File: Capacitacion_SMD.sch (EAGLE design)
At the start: 37 parts, among them IC1 LDO3V3

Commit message: Values corrected for R7 & R8
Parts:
- R4, R5: value 22 -> 470
- R6: value 22 -> 10k
- R7, R8: value 22 -> 22k
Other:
- moved on the sheet: C1, C2, C3, C4, C5, C6, C7, IC1, ISP1, JP1, JP2, LED1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

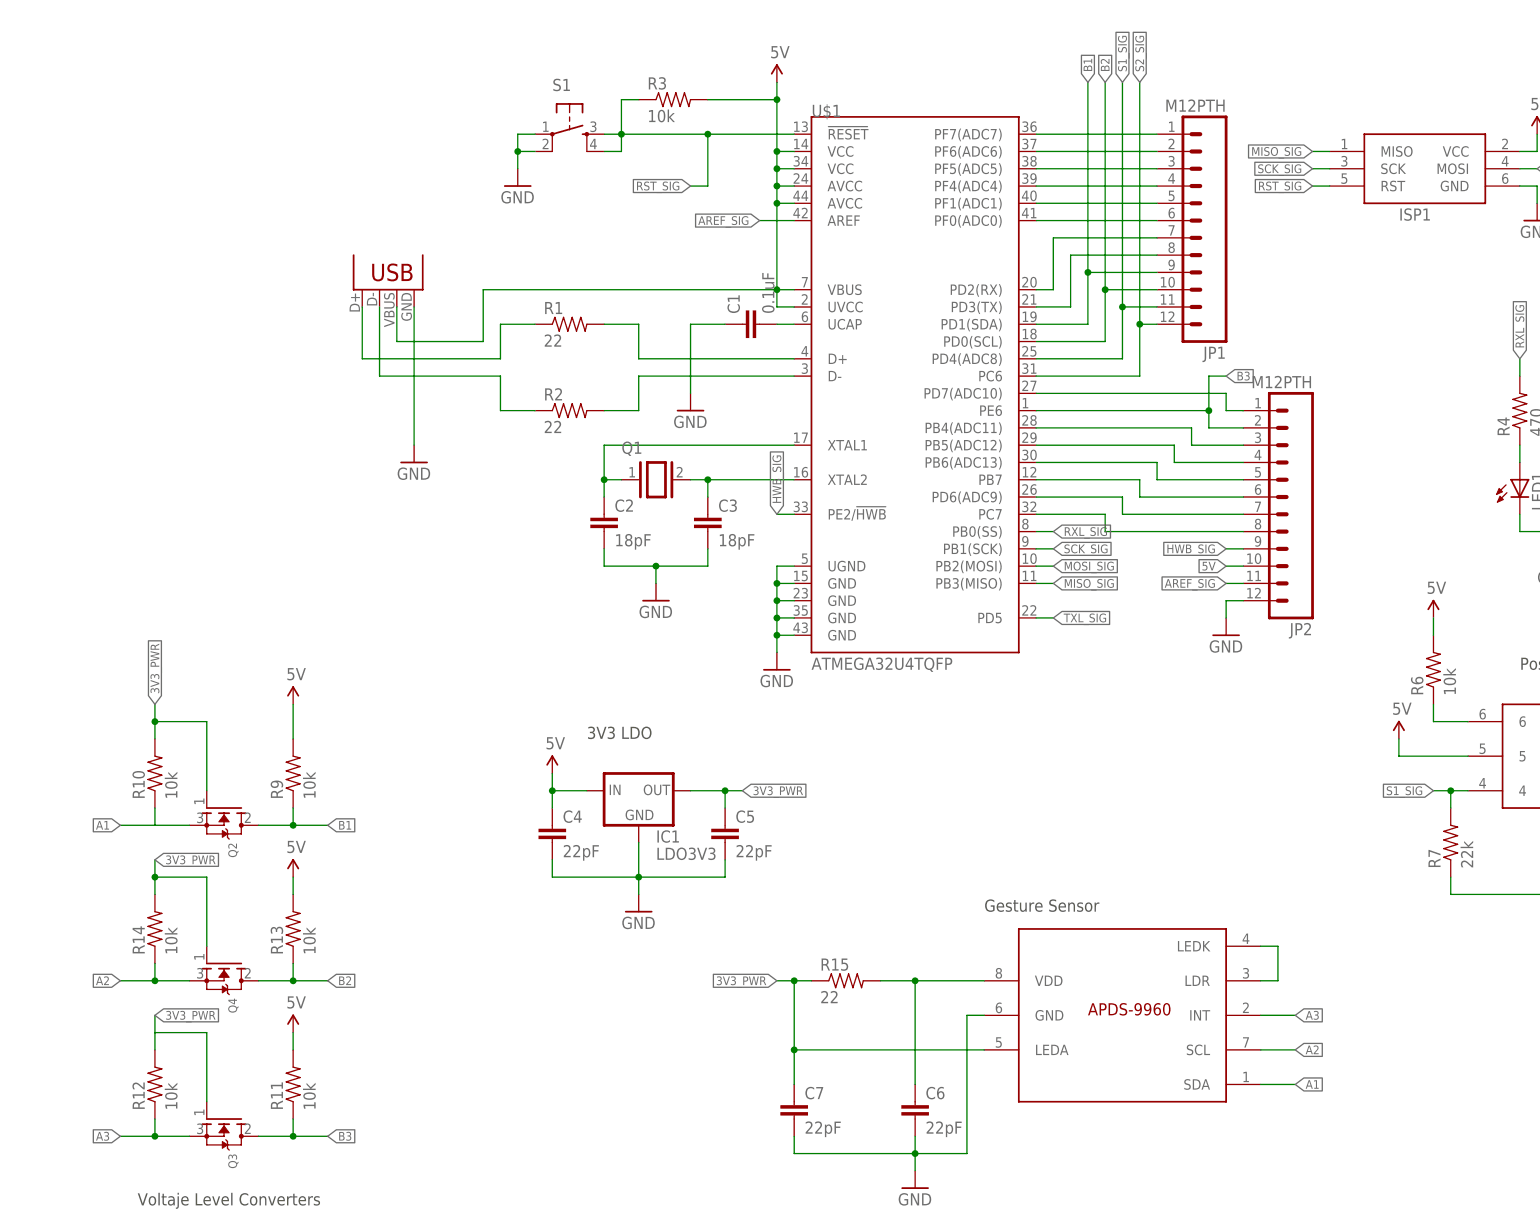
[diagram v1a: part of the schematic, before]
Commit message: Added indicator LEDs
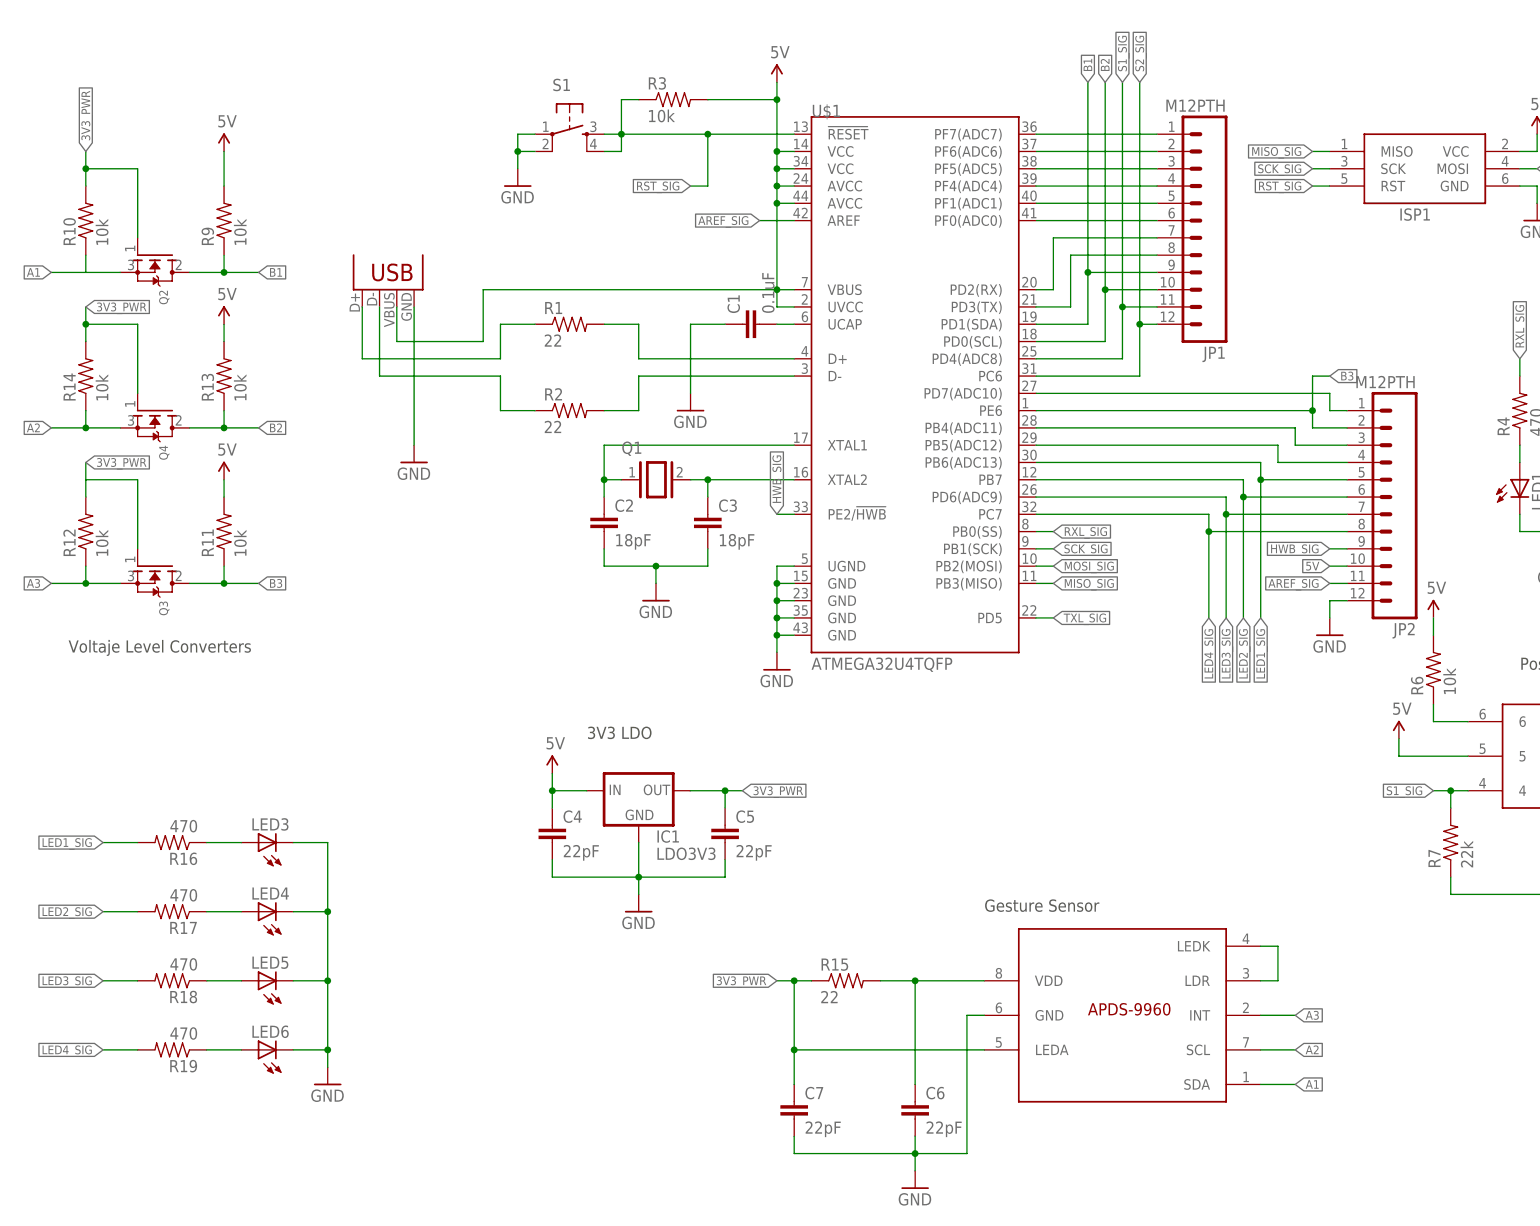
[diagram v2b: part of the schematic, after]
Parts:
- added LED3, LED4, LED5, LED6: (no value), SparkFun-LED:LED5MM
- added R16, R17, R18, R19: 470, SparkFun-Resistors:RESISTORAXIAL-0.3
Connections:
- removed net N$26: JP2.5, U$1.PB6(ADC13)
- removed net N$27: JP2.6, U$1.PB7
- removed net N$28: JP2.7, U$1.PD6(ADC9)
- removed net N$29: JP2.8, U$1.PC7
- new net LED1_SIG: JP2.5, R16.2, U$1.PB6(ADC13)
- new net LED2_SIG: JP2.6, R17.2, U$1.PB7
- new net LED3_SIG: JP2.7, R18.2, U$1.PD6(ADC9)
- new net LED4_SIG: JP2.8, R19.2, U$1.PC7
- new net N$21: LED4.A, R17.1
- new net N$22: LED5.A, R18.1
- new net N$23: LED6.A, R19.1
- new net N$9: LED3.A, R16.1
- net GND: now also LED3.C, LED4.C, LED5.C, LED6.C
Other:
- moved on the sheet: JP2, Q2, Q3, Q4, R10, R11, R12, R13, R14, R9
